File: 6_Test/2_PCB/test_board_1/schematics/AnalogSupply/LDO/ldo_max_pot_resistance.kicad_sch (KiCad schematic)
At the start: 6 parts, among them U1 TPS74501PDRVR

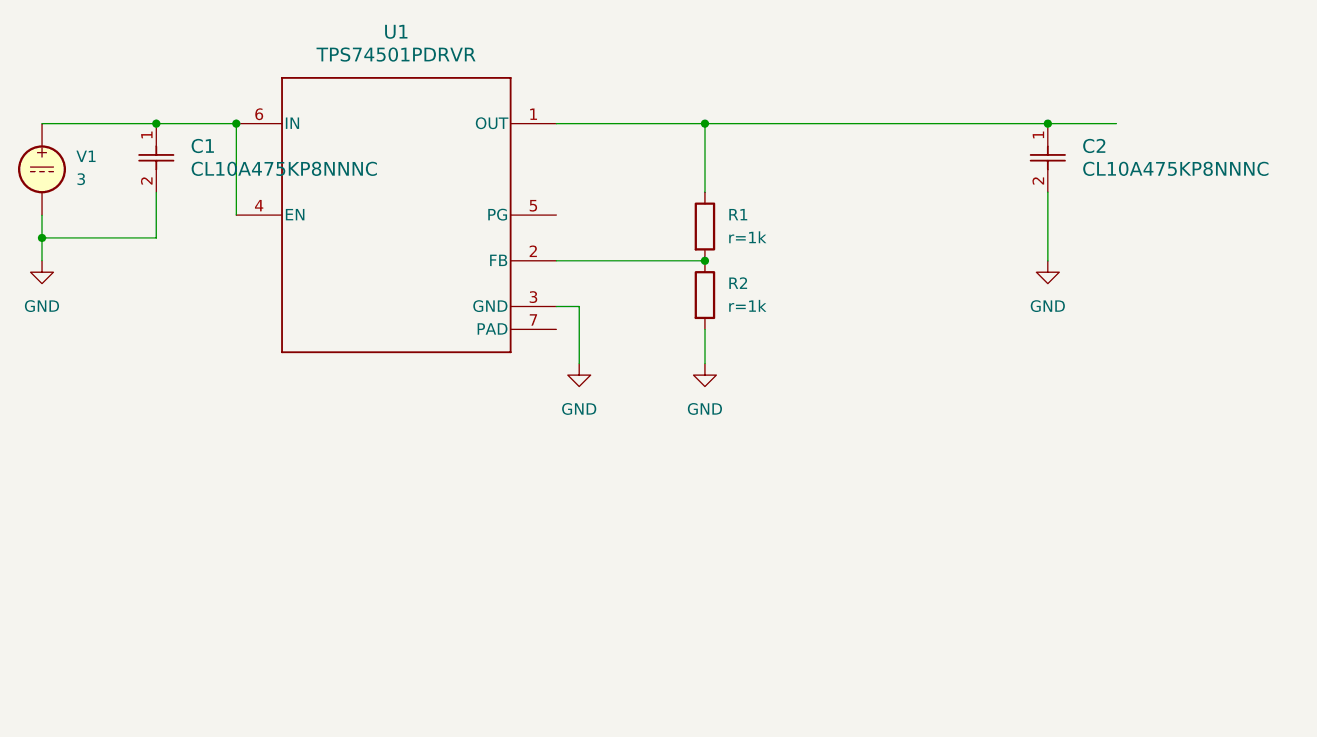
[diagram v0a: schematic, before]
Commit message: ldo simulations done
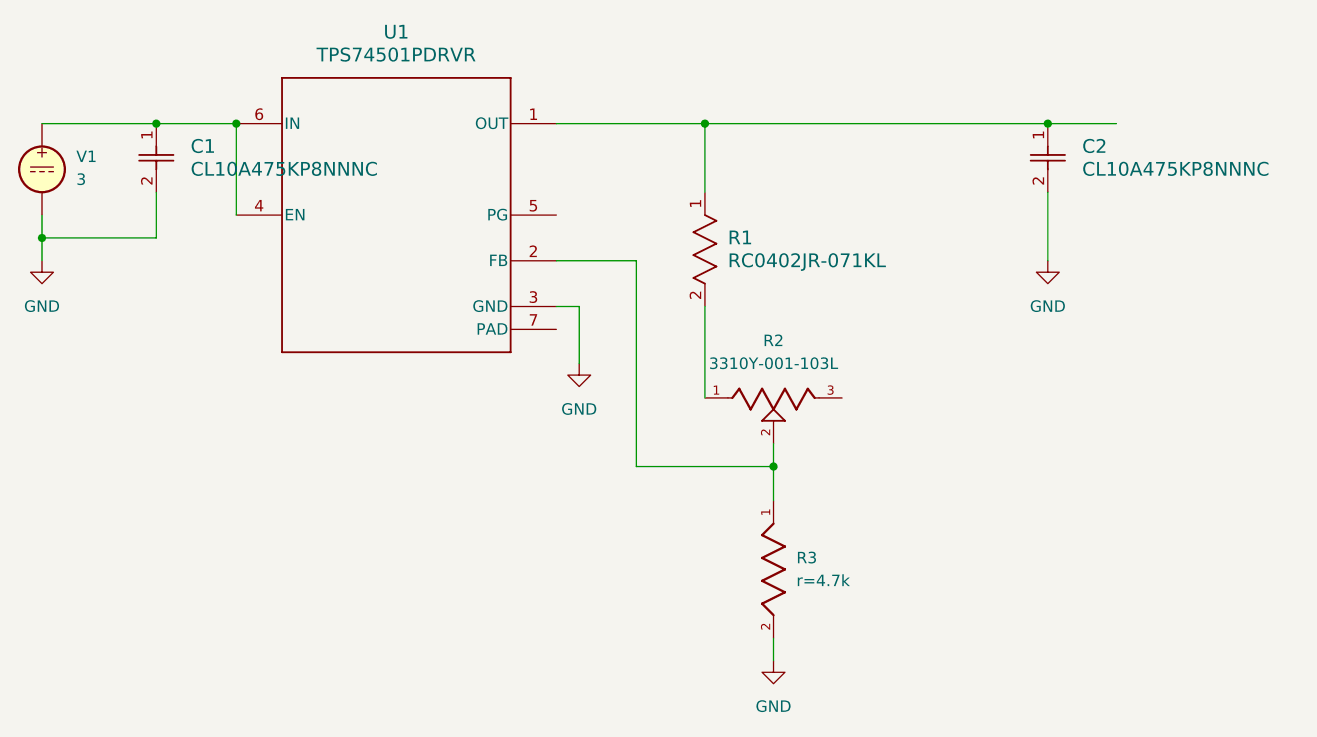
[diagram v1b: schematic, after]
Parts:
- removed R1, R2: ${SIM.PARAMS}, symbol Device:R
- added R1: RC0402JR-071KL, RC0402N_YAG, symbol Resistor1k:RC0402JR-071KL
- added R2: 3310Y-001-103L, 3310Y-001-103L:TRIM_3310Y-001-103L, symbol potentiometer:3310Y-001-103L
- added R3: ${SIM.PARAMS}, RC0402FR-074K7L:RESC1005X40, symbol resistor4.7k:RC0402FR-074K7L
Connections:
- net GND: now also R3.2
- net at C2.1, U1.1 (OUT): now also R1.1
- net at U1.2 (FB): now also R2.2, R3.1
- new net: R1.2, R2.1
